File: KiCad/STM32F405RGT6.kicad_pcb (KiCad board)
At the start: 4 copper layers, 101.6 x 101.6 mm, 52 parts, among them IC1 FT232RQ-REEL, J1 USB_C_Receptacle_USB2.0, J2 USB_C_Receptacle_USB2.0, J201 Conn_02x32_Odd_Even, J202 Conn_02x20_Odd_Even, U1 STM32F405RGTx, U2 AT24CS64-SSHM, Y1 25MHz

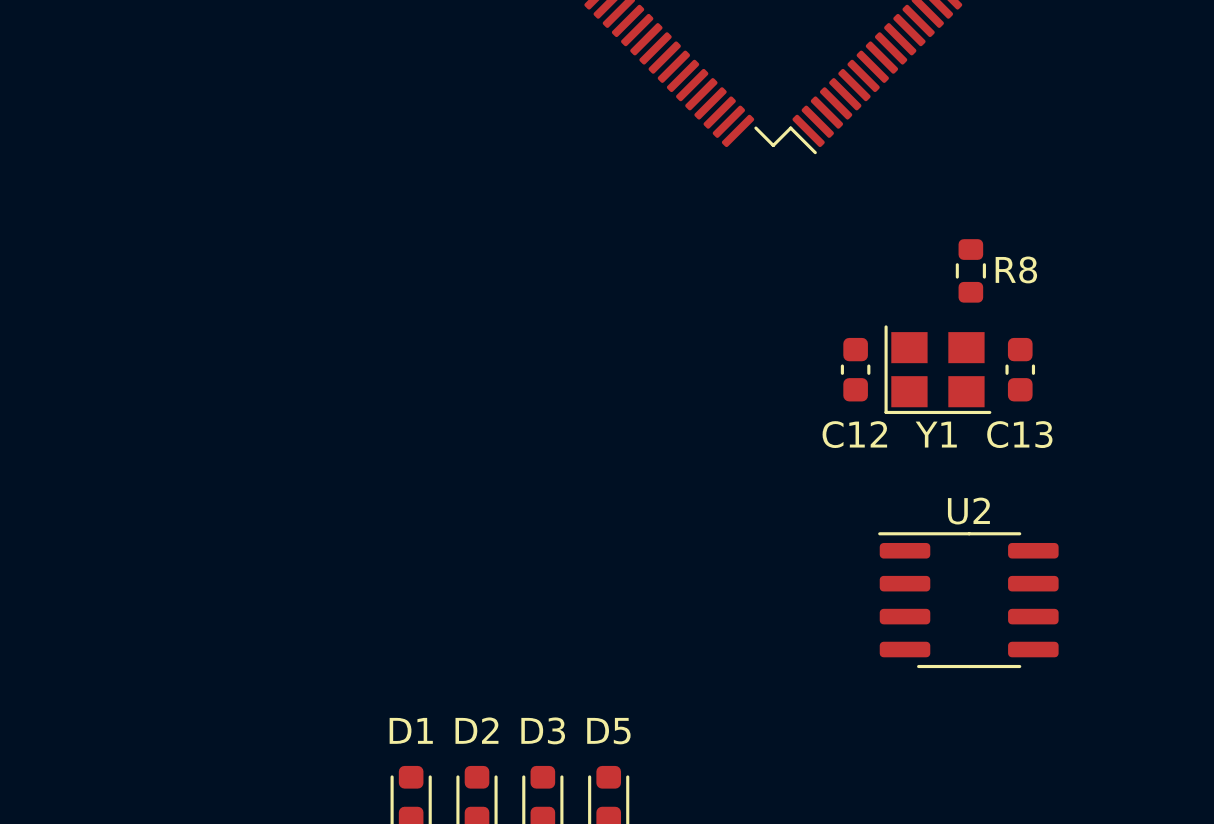
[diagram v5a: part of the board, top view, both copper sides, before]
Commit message: Updated STM32 Cube and KiCad files
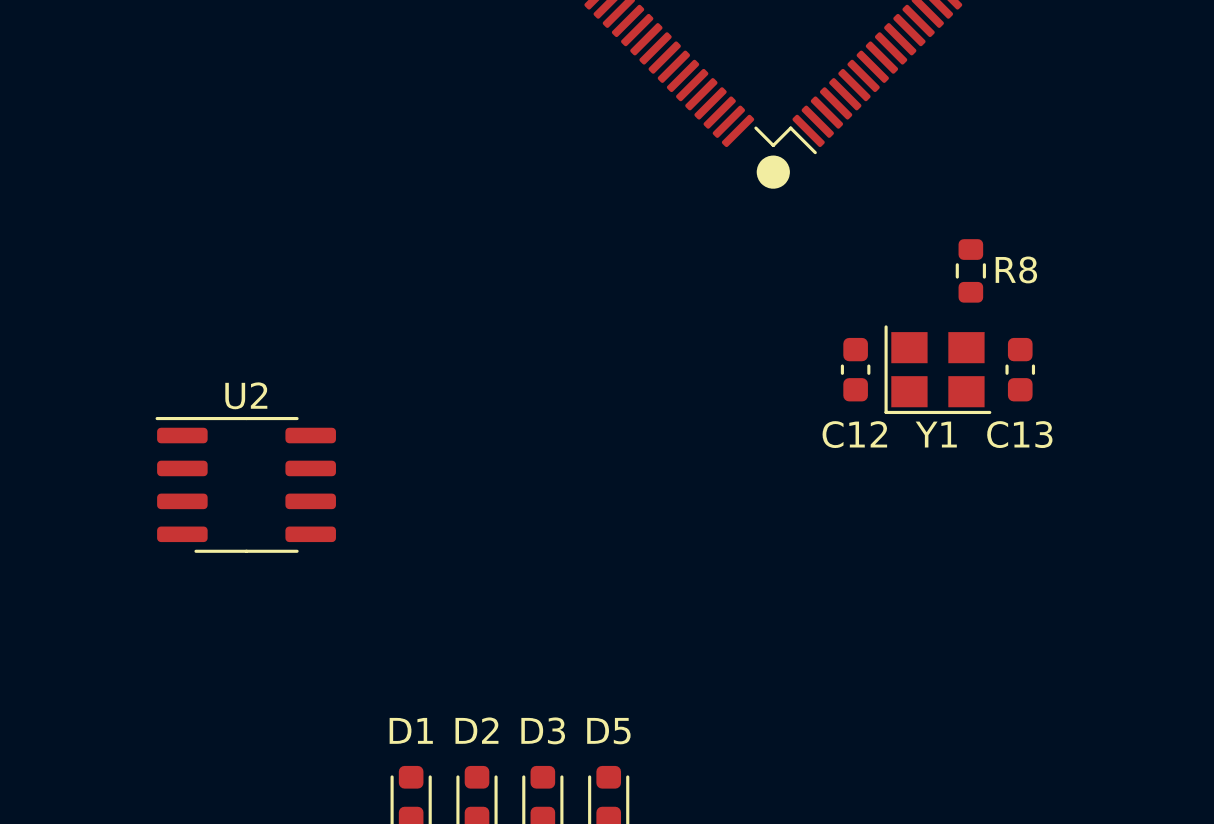
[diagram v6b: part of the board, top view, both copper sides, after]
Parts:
- moved U2 28.2 mm to (124.6, 105.1)
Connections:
- IC1 pad 31: FTDI_DTR -> unconnected-(IC1-Pad31)
- IC1 pad 32: unconnected-(IC1-Pad32) -> FTDI_RTS
- U1 pad 10: unconnected-(U1-Pad10) -> +A6
- U1 pad 11: unconnected-(U1-Pad11) -> +A5
- U1 pad 14: unconnected-(U1-Pad14) -> +A1
- U1 pad 15: unconnected-(U1-Pad15) -> +A2
- U1 pad 16: unconnected-(U1-Pad16) -> +A3
- U1 pad 17: unconnected-(U1-Pad17) -> +A4
- U1 pad 2: unconnected-(U1-Pad2) -> GPIO10
- U1 pad 20: unconnected-(U1-Pad20) -> +A9
- U1 pad 21: unconnected-(U1-Pad21) -> +A10
- U1 pad 22: unconnected-(U1-Pad22) -> GPIO13
- U1 pad 23: unconnected-(U1-Pad23) -> GPIO14
- U1 pad 24: unconnected-(U1-Pad24) -> GPIO15~
- U1 pad 25: unconnected-(U1-Pad25) -> GPIO16~
- U1 pad 26: unconnected-(U1-Pad26) -> GPIO17~
- U1 pad 27: unconnected-(U1-Pad27) -> GPIO18~
- U1 pad 29: unconnected-(U1-Pad29) -> TX1
- U1 pad 3: unconnected-(U1-Pad3) -> GPIO11
- U1 pad 30: unconnected-(U1-Pad30) -> RX1
- U1 pad 33: unconnected-(U1-Pad33) -> GPIO19~
- U1 pad 34: unconnected-(U1-Pad34) -> GPIO20~
- U1 pad 37: unconnected-(U1-Pad37) -> GPIO1~
- U1 pad 38: unconnected-(U1-Pad38) -> GPIO2~
- U1 pad 39: unconnected-(U1-Pad39) -> GPIO3~
- U1 pad 4: unconnected-(U1-Pad4) -> GPIO12
- U1 pad 40: unconnected-(U1-Pad40) -> GPIO4~
- U1 pad 41: unconnected-(U1-Pad41) -> GPIO5
- U1 pad 44: unconnected-(U1-Pad44) -> FTDI_RTS
- U1 pad 45: unconnected-(U1-Pad45) -> FTDI_CTS
- U1 pad 46: unconnected-(U1-Pad46) -> SWDIO
- U1 pad 49: unconnected-(U1-Pad49) -> SWCLK
- U1 pad 50: unconnected-(U1-Pad50) -> GPIO6
- U1 pad 51: unconnected-(U1-Pad51) -> SCLK1
- U1 pad 52: unconnected-(U1-Pad52) -> MISO1
- U1 pad 53: unconnected-(U1-Pad53) -> MOSI1
- U1 pad 54: unconnected-(U1-Pad54) -> CS1
- U1 pad 55: unconnected-(U1-Pad55) -> SWO
- U1 pad 56: unconnected-(U1-Pad56) -> CS2
- U1 pad 57: unconnected-(U1-Pad57) -> GPIO7
- U1 pad 58: unconnected-(U1-Pad58) -> GPIO8
- U1 pad 59: unconnected-(U1-Pad59) -> GPIO9
- U1 pad 61: unconnected-(U1-Pad61) -> SCL1
- U1 pad 62: unconnected-(U1-Pad62) -> SDA1
- U1 pad 8: unconnected-(U1-Pad8) -> +A8
- U1 pad 9: unconnected-(U1-Pad9) -> +A7
- U2 pad 5: unconnected-(U2-Pad5) -> SDA1
- U2 pad 6: unconnected-(U2-Pad6) -> SCL1

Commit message: Update Schematic and PCB
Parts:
- added D10: PRTR5V0U2X, Package_TO_SOT_SMD:SOT-143, F.Cu at (124.6, 46.0)
- added D9: PRTR5V0U2X, Package_TO_SOT_SMD:SOT-143, F.Cu at (165.2, 46.0)
- added FB3: 220R @100MHz, Inductor_SMD:L_0603_1608Metric, F.Cu at (116.8, 42.2)
- added FB4: 220R @100MHz, Inductor_SMD:L_0603_1608Metric, F.Cu at (157.6, 42.2)
- moved D1 14.8 mm to (141.1, 127.9)
- moved R1 14.8 mm to (141.1, 131.8)
- moved D2 14.8 mm to (143.7, 127.9)
- moved D3 14.8 mm to (146.2, 127.9)
- moved D5 14.8 mm to (148.7, 127.9)
- moved R2 14.8 mm to (143.7, 131.8)
- moved R3 14.8 mm to (146.2, 131.8)
- moved R4 14.8 mm to (148.7, 131.8)
- moved D6 1.91 mm to (155.6, 51.7)
- moved D7 1.91 mm to (155.6, 53.6)
- moved IC1 1.91 mm to (165.2, 51.7)
- moved R5 1.91 mm to (159.3, 51.7)
- moved R6 1.91 mm to (159.3, 53.6)
- moved J1 0.40 mm to (124.6, 38.2)
- moved J2 0.40 mm to (165.2, 38.2)
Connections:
- J1 pad A1: Net-(J1-PadA1) -> GND
- J1 pad A12: Net-(J1-PadA1) -> GND
- J1 pad B1: Net-(J1-PadA1) -> GND
- J1 pad B12: Net-(J1-PadA1) -> GND
- J2 pad A1: Net-(J2-PadA1) -> GND
- J2 pad A12: Net-(J2-PadA1) -> GND
- J2 pad B1: Net-(J2-PadA1) -> GND
- J2 pad B12: Net-(J2-PadA1) -> GND

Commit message: Updated PCB and Schematic
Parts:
- removed C14, C15: 100nF, Capacitor_SMD:C_0603_1608Metric
- removed C16: 10uF, Capacitor_SMD:C_0603_1608Metric
- removed D6, D7: Red LED, LED_SMD:LED_0603_1608Metric
- removed D9: PRTR5V0U2X, Package_TO_SOT_SMD:SOT-143
- removed FB4: 220R @100MHz, Inductor_SMD:L_0603_1608Metric
- removed IC1: FT232RQ-REEL, Package_DFN_QFN:QFN-32-1EP_5x5mm_P0.5mm_EP3.3x3.3mm_ThermalVias
- removed J2: USB_C_Receptacle_USB2.0, Connector_USB:USB_C_Receptacle_HRO_TYPE-C-31-M-12
- removed R5, R6: 1k, Resistor_SMD:R_0603_1608Metric
- moved FB3 20.3 mm to (137.1, 42.2)
- moved D10 20.3 mm to (144.9, 46.0)
- moved J1 20.3 mm to (144.9, 38.2)
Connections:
- net Net-(D10-Pad4) renamed /USB_5V
- FB3 pad 1: unconnected-(FB3-Pad1) -> Net-(FB3-Pad1)
